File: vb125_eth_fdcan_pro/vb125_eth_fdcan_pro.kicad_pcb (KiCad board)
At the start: 4 copper layers, 105 x 82 mm, 106 parts, among them J1 TAGconnect NL, J2 ARJM11C7-114-BA-EW2, J3 USB_C_Receptacle_USB2.0, J4 D09P33E4GL00LF, J5 D09P33E4GL00LF, M1 DM-OLED042-647, M2 B0505MT-1WR4, Q1 BSS138, Q2 BSS138, Q3 FDN358P, Q4 FDN358P, SW1 DS04-254-2-03BK-SMT, U1 STM32H725IGKx, U2 LAN8740A, U3 USB3315, U4 AOZ1282CI, U6 RT5760A/B, U7 LT8304IS8E#PBF, U8 ADM3057E, U9 LTC4267, X1 50MHz, X2 24MHz

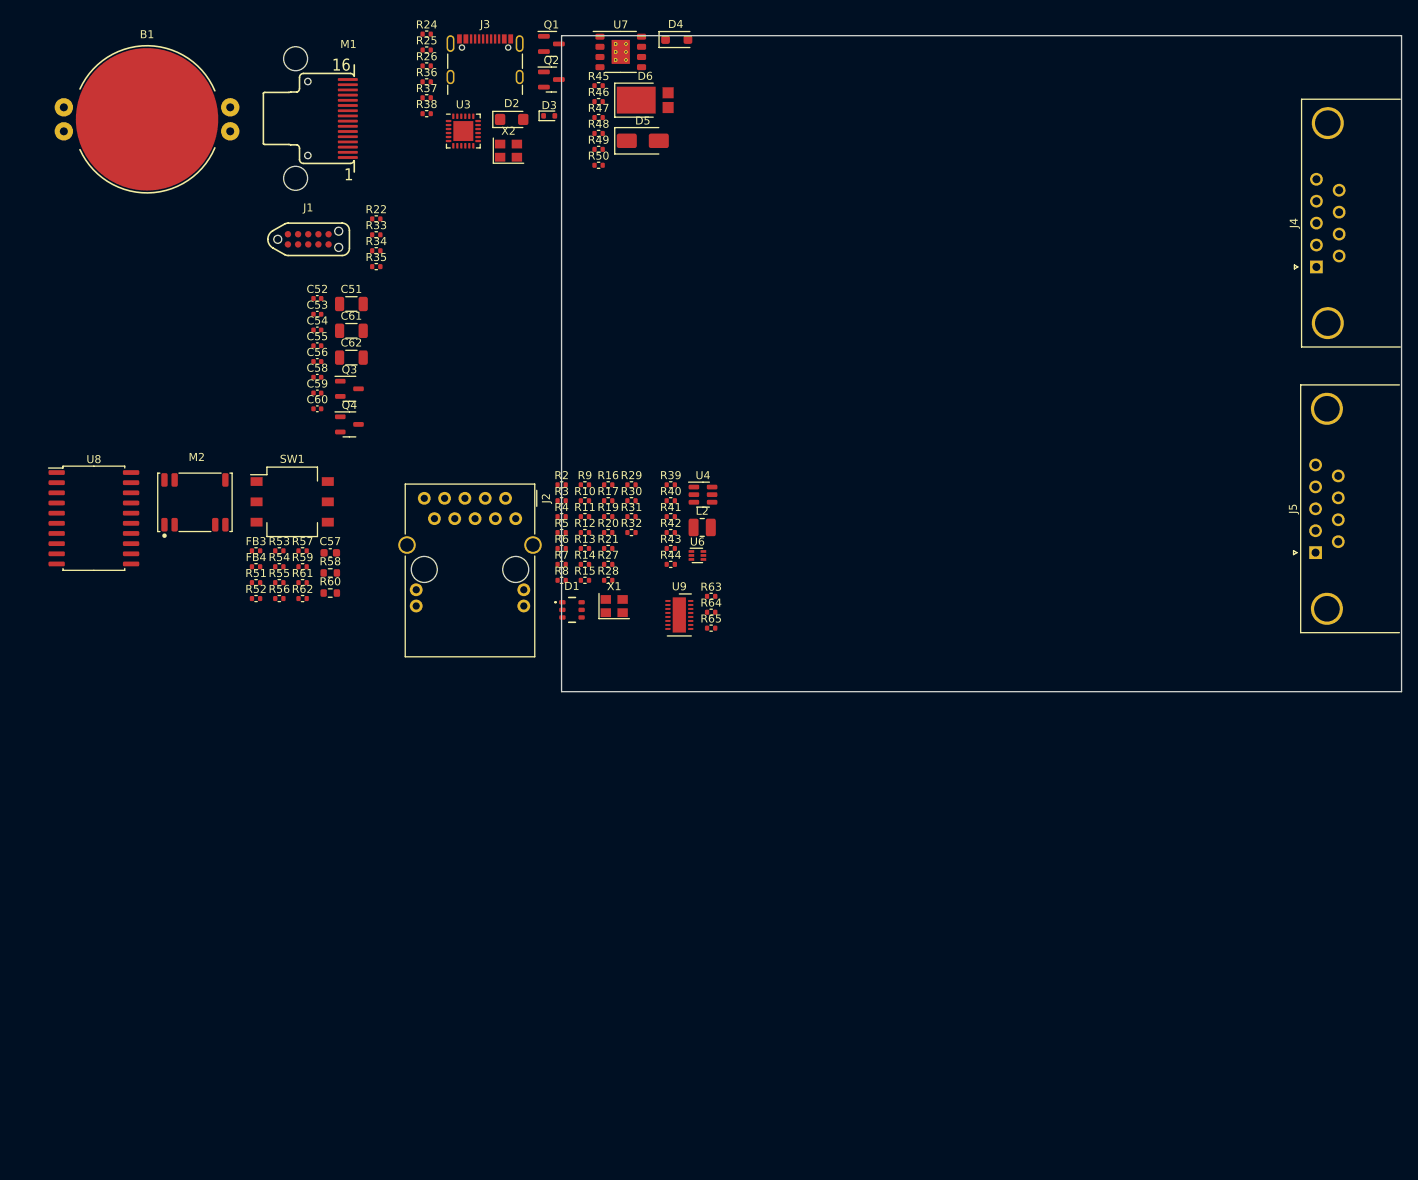
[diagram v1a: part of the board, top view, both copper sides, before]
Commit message: CAN schematics. Assign IO on H7.
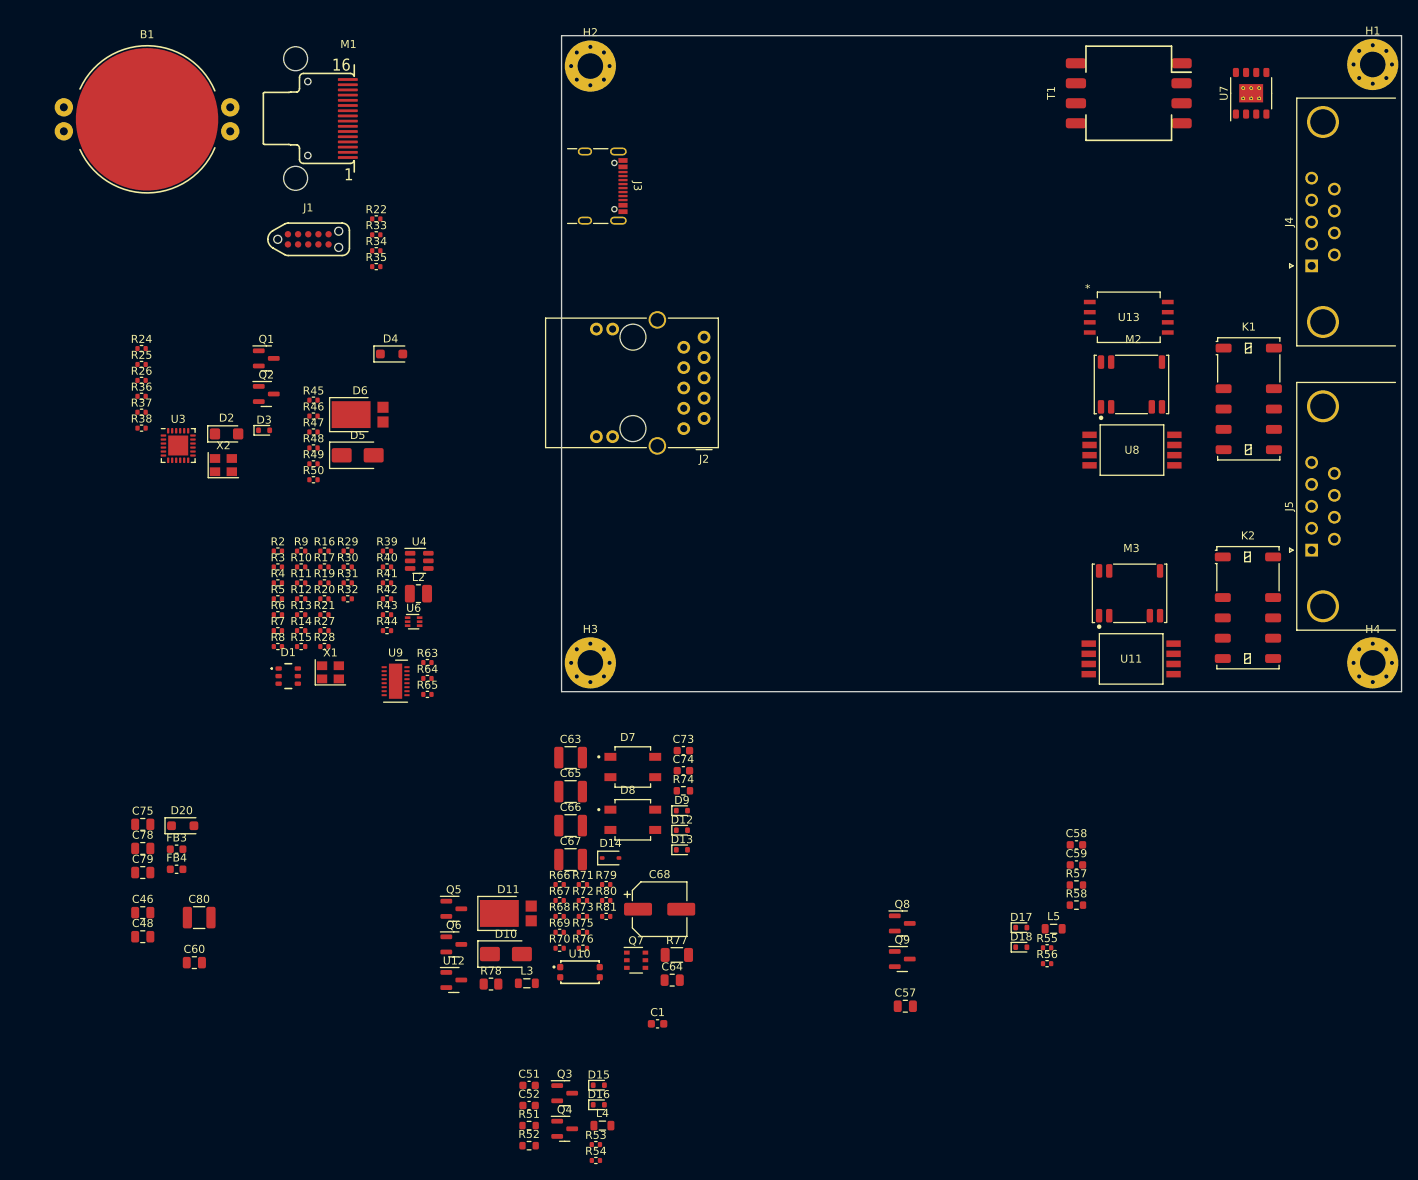
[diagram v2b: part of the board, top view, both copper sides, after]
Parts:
- removed C53, C55: X7R_10nF_50V, Capacitor_SMD:C_0402_1005Metric
- removed C54: 50V_100nF_X7R, Capacitor_SMD:C_0402_1005Metric
- removed C56: 5.0pF, Capacitor_SMD:C_0402_1005Metric
- removed C61, C62: 10.0uF ±10% 10V X7R, Capacitor_SMD:C_1206_3216Metric
- removed R59: 100K 1%, Resistor_SMD:R_0402_1005Metric
- removed R60: 56R, Resistor_SMD:R_0603_1608Metric
- removed R61, R62: 0, Resistor_SMD:R_0402_1005Metric
- removed SW1: DS04-254-2-03BK-SMT, Button_Switch_SMD:SW_DIP_SPSTx03_Slide_Omron_A6S-310x_W8.9mm_P2.54mm
- added C1: 4.7uF, Capacitor_SMD:C_0603_1608Metric, F.Cu at (161.2, 161.3)
- added C46: 10uF, Capacitor_SMD:C_0805_2012Metric, F.Cu at (96.8, 147.4)
- added C48: 10uF, Capacitor_SMD:C_0805_2012Metric, F.Cu at (96.8, 150.4)
- added C63: 4.7uF, Capacitor_SMD:C_1210_3225Metric, F.Cu at (150.3, 128.0)
- added C64: 100nF, Capacitor_SMD:C_0805_2012Metric, F.Cu at (163.0, 155.9)
- added C65: 1uF, Capacitor_SMD:C_1210_3225Metric, F.Cu at (150.3, 132.3)
- added C66: 47uF, Capacitor_SMD:C_1210_3225Metric, F.Cu at (150.3, 136.5)
- added C67: 47uF, Capacitor_SMD:C_1210_3225Metric, F.Cu at (150.3, 140.8)
- added C68: 220uF?, Capacitor_SMD:CP_Elec_6.3x7.7, F.Cu at (161.5, 147.0)
- added C73: 68pF, Capacitor_SMD:C_0603_1608Metric, F.Cu at (164.4, 127.2)
- added C74: 4.7uF, Capacitor_SMD:C_0603_1608Metric, F.Cu at (164.4, 129.7)
- added C75: 10uF, Capacitor_SMD:C_0805_2012Metric, F.Cu at (96.8, 136.4)
- added C78: DNP, Capacitor_SMD:C_0805_2012Metric, F.Cu at (96.8, 139.4)
- added C79: 10uF, Capacitor_SMD:C_0805_2012Metric, F.Cu at (96.8, 142.4)
- added C80: 10uF, Capacitor_SMD:C_1210_3225Metric, F.Cu at (103.9, 148.0)
- added D10: SMAJ58A, Diode_SMD:D_SMA, F.Cu at (142.2, 152.6)
- added D11: PDS360-13, Diode_SMD:D_PowerDI-5, F.Cu at (142.5, 147.5)
- added D12: BAS516, Diode_SMD:D_SOD-523, F.Cu at (164.2, 137.1)
- added D13: BAS516, Diode_SMD:D_SOD-523, F.Cu at (164.2, 139.6)
- added D14: MMSZ5237BS-7-F, Diode_SMD:D_SOD-323, F.Cu at (155.3, 140.6)
- added D15: BAS516, Diode_SMD:D_SOD-523, F.Cu at (153.9, 169.0)
- added D16: BAS516, Diode_SMD:D_SOD-523, F.Cu at (153.9, 171.4)
- added D17: BAS516, Diode_SMD:D_SOD-523, F.Cu at (206.7, 149.3)
- added D18: BAS516, Diode_SMD:D_SOD-523, F.Cu at (206.7, 151.7)
- added D20: RB168MM150TFTR, Diode_SMD:D_SOD-123F, F.Cu at (101.8, 136.6)
- added D7: HDS10M-13, vhrd_passive_diode:DIOB_HDS10M-13, F.Cu at (158.1, 129.2)
- added D8: HDS10M-13, vhrd_passive_diode:DIOB_HDS10M-13, F.Cu at (158.1, 135.8)
- added D9: BAS516, Diode_SMD:D_SOD-523, F.Cu at (164.2, 134.7)
- added H1: MountingHole_Pad, MountingHole:MountingHole_3.2mm_M3_Pad_Via, F.Cu at (250.6, 41.4)
- added H2: MountingHole_Pad, MountingHole:MountingHole_3.2mm_M3_Pad_Via, F.Cu at (152.8, 41.6)
- added H3: MountingHole_Pad, MountingHole:MountingHole_3.2mm_M3_Pad_Via, F.Cu at (152.8, 116.2)
- added H4: MountingHole_Pad, MountingHole:MountingHole_3.2mm_M3_Pad_Via, F.Cu at (250.6, 116.2)
- added K1: EE2-4.5TNUH, vhrd_relay:Relay_DPDT_Kemet_EE2_NUH_DoubleCoil, F.Cu at (235.1, 83.2)
- added K2: EE2-4.5TNUH, vhrd_relay:Relay_DPDT_Kemet_EE2_NUH_DoubleCoil, F.Cu at (235.0, 109.3)
- added L3: 3.3uH, Inductor_SMD:L_0805_2012Metric, F.Cu at (144.9, 156.2)
- added L4: 6.8uH, Inductor_SMD:L_0805_2012Metric, F.Cu at (154.3, 174.0)
- added L5: 6.8uH, Inductor_SMD:L_0805_2012Metric, F.Cu at (210.7, 149.4)
- added M3: B0505MT-1WR4, vhrd_module_power:B0505MT-1WR4, F.Cu at (220.2, 107.5)
- added Q5: 2N7002, Package_TO_SOT_SMD:SOT-23, F.Cu at (135.7, 146.9)
- added Q6: MMBTA42, Package_TO_SOT_SMD:SOT-23, F.Cu at (135.7, 151.4)
- added Q7: Si3440DV, Package_SO:TSOP-6_1.65x3.05mm_P0.95mm, F.Cu at (158.5, 153.4)
- added Q8: BSS138, Package_TO_SOT_SMD:SOT-23, F.Cu at (191.8, 148.8)
- added Q9: BSS138, Package_TO_SOT_SMD:SOT-23, F.Cu at (191.8, 153.2)
- added R66: 470R, Resistor_SMD:R_0402_1005Metric, F.Cu at (149.0, 143.9)
- added R67: 100K, Resistor_SMD:R_0402_1005Metric, F.Cu at (149.0, 145.9)
- added R68: 33K2, Resistor_SMD:R_0402_1005Metric, F.Cu at (149.0, 147.9)
- added R69: 47K, Resistor_SMD:R_0402_1005Metric, F.Cu at (149.0, 149.9)
- added R70: 1K, Resistor_SMD:R_0402_1005Metric, F.Cu at (149.0, 151.9)
- added R71: 10K, Resistor_SMD:R_0402_1005Metric, F.Cu at (151.9, 143.9)
- added R72: 6K8, Resistor_SMD:R_0402_1005Metric, F.Cu at (151.9, 145.9)
- added R73: 100K, Resistor_SMD:R_0402_1005Metric, F.Cu at (151.9, 147.9)
- added R74: 10R, Resistor_SMD:R_0603_1608Metric, F.Cu at (164.4, 132.2)
- added R75: DNP, Resistor_SMD:R_0402_1005Metric, F.Cu at (151.9, 149.9)
- added R76: 510R, Resistor_SMD:R_0402_1005Metric, F.Cu at (151.9, 151.9)
- added R77: 0.125R, Resistor_SMD:R_1206_3216Metric, F.Cu at (163.6, 152.7)
- added R78: 100R, Resistor_SMD:R_0805_2012Metric, F.Cu at (140.4, 156.3)
- added R79: 4K7, Resistor_SMD:R_0402_1005Metric, F.Cu at (154.8, 143.9)
- added R80: 220K, Resistor_SMD:R_0402_1005Metric, F.Cu at (154.8, 145.9)
- added R81: 220K, Resistor_SMD:R_0402_1005Metric, F.Cu at (154.8, 147.9)
- added T1: PA1134NL, vhrd_transformer:PA1134NL, F.Cu at (220.1, 45.0)
- added U10: PS2911-1-F3-AX, vhrd_opto_isolator:PS2911, F.Cu at (151.5, 154.9)
- added U11: TLP2270, vhrd_generic:SO8L_TOS, F.Cu at (220.4, 115.7)
- added U12: ZR431, Package_TO_SOT_SMD:SOT-23, F.Cu at (135.7, 155.8)
- added U13: ADM3050EBRIZ, vhrd_generic:RI-8-1_ADI, F.Cu at (220.1, 73.0)
- C51: value 10.0uF ±10% 10V X7R -> 4.7uF; footprint Capacitor_SMD:C_1206_3216Metric -> Capacitor_SMD:C_0603_1608Metric
- C52: value 50V_100nF_X7R -> 4.7uF; footprint Capacitor_SMD:C_0402_1005Metric -> Capacitor_SMD:C_0603_1608Metric
- C57: value 4.7uF ±10% 6.3V -> 10uF; footprint Capacitor_SMD:C_0603_1608Metric -> Capacitor_SMD:C_0805_2012Metric
- C58: value 10.0nF ±10% 50V X7R -> 4.7uF; footprint Capacitor_SMD:C_0402_1005Metric -> Capacitor_SMD:C_0603_1608Metric
- C59: value 0.1uF 10% X7R 50V -> 4.7uF; footprint Capacitor_SMD:C_0402_1005Metric -> Capacitor_SMD:C_0603_1608Metric
- C60: value 220.0nF ±10% 10V X7R -> 10uF; footprint Capacitor_SMD:C_0402_1005Metric -> Capacitor_SMD:C_0805_2012Metric
- D6: value PDS835L-13 -> PDS360-13
- FB3: value 100MHz_1.8KOhm -> BLM18HE152SN1D; footprint Resistor_SMD:R_0402_1005Metric -> Inductor_SMD:L_0603_1608Metric
- FB4: value BLM15BX182SN1D_100MHz_1.8KOhm -> BLM18HE152SN1D; footprint Resistor_SMD:R_0402_1005Metric -> Inductor_SMD:L_0603_1608Metric
- Q3, Q4: value FDN358P -> BSS138; footprint Package_TO_SOT_SMD:SOT-23-3 -> Package_TO_SOT_SMD:SOT-23
- R51, R57: value 0 -> 60R4; footprint Resistor_SMD:R_0402_1005Metric -> Resistor_SMD:R_0603_1608Metric
- R52: value 47K 1% -> 60R4; footprint Resistor_SMD:R_0402_1005Metric -> Resistor_SMD:R_0603_1608Metric
- R53, R55: value 0 -> 1K
- R54: value 47K 1% -> 1K
- R56: value 100K 1% -> 1K
- R58: value 56R -> 60R4
- U8: value ADM3057E -> TLP2270; footprint Package_SO:SOIC-20W_7.5x12.8mm_P1.27mm -> vhrd_generic:SO8L_TOS
- moved U8 130.0 mm to (220.5, 89.6)
- moved M2 118.0 mm to (220.4, 81.4)
- moved C59 111.7 mm to (213.6, 141.5)
- moved C58 111.4 mm to (213.6, 138.9)
- moved R55 106.3 mm to (209.9, 151.8)
- moved R56 106.3 mm to (209.9, 153.8)
- moved R57 105.4 mm to (213.6, 144.0)
- moved C52 104.3 mm to (145.1, 171.5)
- moved R58 102.1 mm to (213.6, 146.5)
- moved C51 100.2 mm to (145.1, 169.0)
- moved Q3 92.1 mm to (149.6, 170.0)
- moved Q4 92.1 mm to (149.6, 174.4)
- moved C57 91.5 mm to (192.2, 159.1)
- moved R53 84.1 mm to (153.5, 176.4)
- moved R54 84.1 mm to (153.5, 178.4)
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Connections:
- net +5V0_DCDC renamed TERM1_EN
- net Net-(D5-A) renamed +VIN_CH1
- C51 pad 1: Net-(U8-VCC) -> Net-(C51-Pad1)
- C52 pad 1: Net-(U8-VCC) -> +5V0_SYS
- C57 pad 1: Net-(C57-Pad1) -> Net-(M2-+VO)
- C57 pad 2: GND -> ISO_1
- C58 pad 1: +5V0_ISO -> +5V0_SYS
- C58 pad 2: ISO -> GND
- C59 pad 1: +5V0_ISO -> Net-(C59-Pad1)
- C59 pad 2: ISO -> GND
- C60 pad 1: Net-(U8-VISOOUT) -> +5V0_ISO_2
- C60 pad 2: ISO -> ISO_2
- FB3 pad 1: Net-(FB3-Pad1) -> +3V3_DCDC
- FB3 pad 2: ISO -> Net-(U13-VDD1)
- FB4 pad 1: Net-(U8-VISOOUT) -> Net-(M2-+VO)
- FB4 pad 2: +5V0_ISO -> +5V0_ISO_1
- J2 pad 1: unconnected-(J2-VC2--Pad1) -> POE_AC4
- J2 pad 2: unconnected-(J2-VC1--Pad2) -> POE_AC2
- J2 pad 6: unconnected-(J2-VC2+-Pad6) -> POE_AC3
- J2 pad 7: unconnected-(J2-VC1+-Pad7) -> POE_AC1
- J2 pad SH: unconnected-(J2-SHIELD-PadSH) -> CHASSIS
- J3 pad S1: unconnected-(J3-SHIELD-PadS1) -> CHASSIS
- J4 pad 0: unconnected-(J4-PAD-Pad0) -> CHASSIS
- J4 pad 1: unconnected-(J4-Pad1) -> Net-(D20-A)
- J4 pad 2: unconnected-(J4-Pad2) -> /CAN Ch1/CAN1_L
- J4 pad 3: unconnected-(J4-Pad3) -> ISO_1
- J4 pad 6: unconnected-(J4-Pad6) -> ISO_1
- J4 pad 7: unconnected-(J4-Pad7) -> /CAN Ch1/CAN1_H
- J4 pad 9: unconnected-(J4-Pad9) -> Net-(D20-A)
- J5 pad 0: unconnected-(J5-PAD-Pad0) -> CHASSIS
- M2 pad 13: Net-(C57-Pad1) -> Net-(C51-Pad1)
- M2 pad 14: Net-(C57-Pad1) -> Net-(C51-Pad1)
- M2 pad 6: ISO -> ISO_1
- M2 pad 7: ISO -> ISO_1
- M2 pad 8: +5V -> Net-(M2-+VO)
- Q3 pad 1: /CAN Ch1/TERM_EN_ISO -> /CAN Ch1/CT1_GS
- Q3 pad 2: Net-(Q3-S) -> ISO_1
- Q3 pad 3: Net-(Q3-D) -> Net-(D15-A)
- Q4 pad 1: /CAN Ch1/TERM_EN_ISO -> /CAN Ch1/CT1_GR
- Q4 pad 2: Net-(Q4-S) -> ISO_1
- Q4 pad 3: Net-(Q3-S) -> Net-(D16-A)
- R46 pad 2: ISO -> ISO_1
- R47 pad 2: ISO -> ISO_1
- R51 pad 1: +3V3_DCDC -> /CAN Ch1/CAN1_H
- R51 pad 2: Net-(U8-VCC) -> Net-(K1-Pad5)
- R52 pad 1: Net-(R52-Pad1) -> /CAN Ch1/CAN1_L
- R52 pad 2: ISO -> Net-(K1-Pad8)
- R53 pad 2: Net-(U8-VCC) -> /CAN Ch1/CT1_AS
- R54 pad 1: Net-(R54-Pad1) -> TERM1_DIS
- R54 pad 2: ISO -> /CAN Ch1/CT1_AR
- R55 pad 1: +3V3_DCDC -> TERM2_EN
- R55 pad 2: Net-(U8-VIO) -> /CAN Ch2/CT2_AS
- R56 pad 1: /CAN Ch1/TERM_EN_ISO -> TERM2_DIS
- R56 pad 2: ISO -> /CAN Ch2/CT2_AR
- R57 pad 1: Net-(U8-VIO) -> unconnected-(R57-Pad1)
- R57 pad 2: GND -> Net-(K2-Pad5)
- R58 pad 1: /CAN Ch1/CANL -> unconnected-(R58-Pad1)
- R58 pad 2: Net-(Q3-D) -> Net-(K2-Pad8)
- R63 pad 1: GND -> ISO_POE
- R64 pad 1: GND -> ISO_POE
- R65 pad 1: GND -> ISO_POE
- U7 pad 4: ISO -> ISO_1
- U7 pad 9: ISO -> ISO_1
- U8 pad 1: GND -> /CAN Ch1/CT1_AS
- U8 pad 3: Net-(U8-VCC) -> GND
- U8 pad 4: Net-(U8-VIO) -> /CAN Ch1/CT1_AR
- U8 pad 5: CAN1_RXD -> ISO_1
- U8 pad 6: CAN1_SILENT -> /CAN Ch1/CT1_GR
- U8 pad 7: CAN1_TXD -> /CAN Ch1/CT1_GS
- U8 pad 8: CAN1_STBY -> +5V0_ISO_1
- U9 pad 1: unconnected-(U9-ITH/RUN-Pad1) -> /PoE/POE_ITH
- U9 pad 10: unconnected-(U9-POUT-Pad10) -> ISO_POE
- U9 pad 11: unconnected-(U9-~{PWRGD}-Pad11) -> /PoE/~{POE_PWRGD}
- U9 pad 12: unconnected-(U9-SIGDISA-Pad12) -> /PoE/POE_BR_N
- U9 pad 13: unconnected-(U9-VPORTP-Pad13) -> /PoE/POE_VPORTP
- U9 pad 14: unconnected-(U9-SENSE-Pad14) -> /PoE/POE_ISENSE
- U9 pad 15: unconnected-(U9-PGND-Pad15) -> ISO_POE
- U9 pad 16: unconnected-(U9-VFB-Pad16) -> ISO_POE
- U9 pad 17: unconnected-(U9-EP_PGND-Pad17) -> /PoE/POE_EP_THPAD
- U9 pad 2: unconnected-(U9-PGND-Pad2) -> ISO_POE
- U9 pad 3: unconnected-(U9-NGATE-Pad3) -> /PoE/POE_NGATE
- U9 pad 4: unconnected-(U9-PVCC-Pad4) -> /PoE/POE_PVCC
- U9 pad 5: unconnected-(U9-RCLASS-Pad5) -> Net-(U9-RCLASS)
- U9 pad 7: unconnected-(U9-VPORTN-Pad7) -> /PoE/POE_BR_N

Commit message: Finish schematics.
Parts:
- removed Q8, Q9: BSS138, Package_TO_SOT_SMD:SOT-23
- added C10: 4.7uF, Capacitor_SMD:C_0402_1005Metric, F.Cu at (41.7, 110.0)
- added C100: 1uF, Capacitor_SMD:C_0402_1005Metric, F.Cu at (71.5, 136.3)
- added C101: Y rated, THT, Capacitor_THT:C_Disc_D7.0mm_W2.5mm_P5.00mm, F.Cu at (35.2, 134.5)
- added C102: Y rated, THT, Capacitor_THT:C_Disc_D7.0mm_W2.5mm_P5.00mm, F.Cu at (58.4, 129.4)
- added C103: Y rated, SMD 1808, vhrd_generic:C_1808_4520Metric, F.Cu at (37.0, 139.0)
- added C104: Y rated, SMD 1808, vhrd_generic:C_1808_4520Metric, F.Cu at (60.1, 133.9)
- added C105: 100nF, Capacitor_SMD:C_0402_1005Metric, F.Cu at (72.4, 116.3)
- added C106: 100nF, Capacitor_SMD:C_0402_1005Metric, F.Cu at (72.4, 118.3)
- added C107: 4.7uF, Capacitor_SMD:C_1210_3225Metric, F.Cu at (56.5, 105.2)
- added C108: 4.7uF, Capacitor_SMD:C_1210_3225Metric, F.Cu at (56.5, 109.4)
- added C109: 4.7uF, Capacitor_SMD:C_1210_3225Metric, F.Cu at (56.5, 113.7)
- added C11: 100nF, Capacitor_SMD:C_0402_1005Metric, F.Cu at (41.7, 111.9)
- added C110: 4.7uF, Capacitor_SMD:C_1210_3225Metric, F.Cu at (56.5, 117.9)
- added C111: 100nF, Capacitor_SMD:C_0402_1005Metric, F.Cu at (72.4, 120.3)
- added C112: 100uF, Capacitor_SMD:C_1210_3225Metric, F.Cu at (56.5, 122.2)
- added C113: Y rated, THT, Capacitor_THT:C_Disc_D7.0mm_W2.5mm_P5.00mm, F.Cu at (21.4, 142.1)
- added C114: Y rated, SMD 1808, vhrd_generic:C_1808_4520Metric, F.Cu at (23.1, 146.6)
- added C12: 2.2uF, Capacitor_SMD:C_0402_1005Metric, F.Cu at (41.7, 113.9)
- added C13: 100nF, Capacitor_SMD:C_0402_1005Metric, F.Cu at (41.7, 115.9)
- added C14: 4.7uF, Capacitor_SMD:C_0402_1005Metric, F.Cu at (44.5, 104.0)
- added C15: 10nF, Capacitor_SMD:C_0402_1005Metric, F.Cu at (71.5, 144.2)
- added C16: 10nF, Capacitor_SMD:C_0402_1005Metric, F.Cu at (68.6, 128.4)
- added C17: 22nF, Capacitor_SMD:C_0402_1005Metric, F.Cu at (74.3, 140.3)
- added C18: 100nF, Capacitor_SMD:C_0402_1005Metric, F.Cu at (74.3, 142.2)
- added C19: 4.7uF, Capacitor_SMD:C_0402_1005Metric, F.Cu at (74.3, 144.2)
- added C2: 100nF, Capacitor_SMD:C_0402_1005Metric, F.Cu at (41.7, 104.0)
- added C20: 100nF, Capacitor_SMD:C_0402_1005Metric, F.Cu at (44.5, 106.0)
- added C21: 100nF, Capacitor_SMD:C_0402_1005Metric, F.Cu at (44.5, 108.0)
- added C22: 100nF, Capacitor_SMD:C_0402_1005Metric, F.Cu at (44.5, 110.0)
- added C23: 100nF, Capacitor_SMD:C_0402_1005Metric, F.Cu at (44.5, 111.9)
- added C24: 100nF, Capacitor_SMD:C_0402_1005Metric, F.Cu at (44.5, 113.9)
- added C25: 100nF, Capacitor_SMD:C_0402_1005Metric, F.Cu at (44.5, 115.9)
- added C26: 100nF, Capacitor_SMD:C_0402_1005Metric, F.Cu at (47.4, 104.0)
- added C27: 100nF, Capacitor_SMD:C_0402_1005Metric, F.Cu at (47.4, 106.0)
- added C28: 100nF, Capacitor_SMD:C_0402_1005Metric, F.Cu at (47.4, 108.0)
- added C29: 100nF, Capacitor_SMD:C_0402_1005Metric, F.Cu at (47.4, 110.0)
- added C3: 100nF, Capacitor_SMD:C_0402_1005Metric, F.Cu at (68.6, 140.3)
- added C30: 1uF, Capacitor_SMD:C_0402_1005Metric, F.Cu at (47.4, 111.9)
- added C31: 4.7uF, Capacitor_SMD:C_0402_1005Metric, F.Cu at (47.4, 113.9)
- added C32: 4.7uF, Capacitor_SMD:C_0402_1005Metric, F.Cu at (47.4, 115.9)
- added C33: 220pF, Capacitor_SMD:C_0402_1005Metric, F.Cu at (50.3, 104.0)
- added C34: 10uF, Capacitor_SMD:C_0402_1005Metric, F.Cu at (50.3, 106.0)
- added C35: 10uF, Capacitor_SMD:C_0402_1005Metric, F.Cu at (50.3, 108.0)
- added C36: 1uF, Capacitor_SMD:C_0402_1005Metric, F.Cu at (50.3, 110.0)
- added C37: 100nF, Capacitor_SMD:C_0402_1005Metric, F.Cu at (50.3, 111.9)
- added C38: 10nF, Capacitor_SMD:C_0402_1005Metric, F.Cu at (68.6, 130.4)
- added C39: 10nF, Capacitor_SMD:C_0402_1005Metric, F.Cu at (68.6, 132.3)
- added C4: 100nF, Capacitor_SMD:C_0402_1005Metric, F.Cu at (68.6, 142.2)
- added C40: 10nF, Capacitor_SMD:C_0402_1005Metric, F.Cu at (68.6, 134.3)
- added C41: 10nF, Capacitor_SMD:C_0402_1005Metric, F.Cu at (68.6, 136.3)
- added C42: 3.3nF, Capacitor_SMD:C_0402_1005Metric, F.Cu at (55.2, 142.2)
- added C43: >10uF, Capacitor_SMD:C_0603_1608Metric, F.Cu at (58.6, 142.5)
- added C44: DNP, Capacitor_SMD:C_0603_1608Metric, F.Cu at (58.6, 145.0)
- added C45: 100nF, Capacitor_SMD:C_0402_1005Metric, F.Cu at (55.2, 144.2)
- added C47: DNP, Capacitor_SMD:C_0402_1005Metric, F.Cu at (55.2, 146.2)
- added C49: 1uF, Capacitor_SMD:C_0402_1005Metric, F.Cu at (72.4, 114.3)
- added C5: 100nF, Capacitor_SMD:C_0402_1005Metric, F.Cu at (68.6, 144.2)
- added C50: 220pF, Capacitor_SMD:C_0603_1608Metric, F.Cu at (70.5, 106.7)
- added C53: 4n7, Capacitor_SMD:C_0402_1005Metric, F.Cu at (32.0, 133.5)
- added C54: 100nF, Capacitor_SMD:C_0402_1005Metric, F.Cu at (32.0, 135.5)
- added C55: DNP, Capacitor_SMD:C_0805_2012Metric, F.Cu at (41.7, 36.8)
- added C56: 10uF, Capacitor_SMD:C_0805_2012Metric, F.Cu at (41.7, 39.8)
- added C6: 1uF, Capacitor_SMD:C_0402_1005Metric, F.Cu at (71.5, 140.3)
- added C61: 100nF, Capacitor_SMD:C_0402_1005Metric, F.Cu at (32.0, 137.4)
- added C62: 10nF, Capacitor_SMD:C_0402_1005Metric, F.Cu at (32.0, 139.4)
- added C69: 33nF, Capacitor_SMD:C_0402_1005Metric, F.Cu at (45.5, 133.5)
- added C7: 470pF, Capacitor_SMD:C_0402_1005Metric, F.Cu at (71.5, 142.2)
- added C70: 1uF, Capacitor_SMD:C_0402_1005Metric, F.Cu at (45.5, 135.5)
- added C71: 27nF, Capacitor_SMD:C_0402_1005Metric, F.Cu at (45.5, 137.4)
- added C72: 470pF, Capacitor_SMD:C_0402_1005Metric, F.Cu at (45.5, 139.4)
- added C76: 10nF, Capacitor_SMD:C_0402_1005Metric, F.Cu at (32.0, 141.4)
- added C77: 100nF, Capacitor_SMD:C_0402_1005Metric, F.Cu at (32.0, 143.3)
- added C8: 1uF, Capacitor_SMD:C_0402_1005Metric, F.Cu at (41.7, 106.0)
- added C81: 4.7uF, Capacitor_SMD:C_0603_1608Metric, F.Cu at (17.7, 93.7)
- added C82: 100nF, Capacitor_SMD:C_0402_1005Metric, F.Cu at (50.3, 113.9)
- added C83: 12pF, Capacitor_SMD:C_0402_1005Metric, F.Cu at (24.3, 86.1)
- added C84: 12pF, Capacitor_SMD:C_0402_1005Metric, F.Cu at (24.3, 88.1)
- added C85: 1uF, Capacitor_SMD:C_0402_1005Metric, F.Cu at (71.5, 128.4)
- added C86: 100nF, Capacitor_SMD:C_0402_1005Metric, F.Cu at (71.5, 130.4)
- added C87: 4.7uF, Capacitor_SMD:C_0603_1608Metric, F.Cu at (53.8, 36.6)
- added C88: 100nF, Capacitor_SMD:C_0402_1005Metric, F.Cu at (71.5, 132.3)
- added C89: 100uF, Capacitor_SMD:C_1210_3225Metric, F.Cu at (55.7, 77.3)
- added C9: 1uF, Capacitor_SMD:C_0402_1005Metric, F.Cu at (41.7, 108.0)
- added C90: 100uF, Capacitor_SMD:C_1210_3225Metric, F.Cu at (55.7, 81.5)
- added C91: 100uF, Capacitor_SMD:C_1210_3225Metric, F.Cu at (55.7, 85.8)
- added C92: 4.7uF, Capacitor_SMD:C_0603_1608Metric, F.Cu at (18.4, 60.4)
- added C93: 100nF, Capacitor_SMD:C_0402_1005Metric, F.Cu at (55.2, 132.3)
- added C94: 10nF, Capacitor_SMD:C_0402_1005Metric, F.Cu at (55.2, 134.3)
- added C95: 10uF, Capacitor_SMD:C_0805_2012Metric, F.Cu at (41.7, 42.9)
- added C96: 100nF, Capacitor_SMD:C_0402_1005Metric, F.Cu at (55.2, 136.3)
- added C97: 10uF, Capacitor_SMD:C_0805_2012Metric, F.Cu at (41.7, 45.9)
- added C98: 4n7, Capacitor_SMD:C_0402_1005Metric, F.Cu at (55.2, 138.3)
- added C99: 1uF, Capacitor_SMD:C_0402_1005Metric, F.Cu at (71.5, 134.3)
- added D21: buspower_iso: SMAJ58CA; buspower_dc: SMAJ36CA, Diode_SMD:D_SMA, F.Cu at (235.2, 52.4)
- added D23: PDS360-13, Diode_SMD:D_PowerDI-5, F.Cu at (63.7, 116.2)
- added FB1: MH1608-601Y, Inductor_SMD:L_0603_1608Metric, F.Cu at (69.2, 146.4)
- added FB2: FBMJ1608HM180NTR, Inductor_SMD:L_0603_1608Metric, F.Cu at (42.2, 118.1)
- added FB5: BLM18HE152SN1D, Inductor_SMD:L_0603_1608Metric, F.Cu at (18.4, 62.9)
- added FB6: BLM18HE152SN1D, Inductor_SMD:L_0603_1608Metric, F.Cu at (18.4, 65.4)
- added J6: MEM2061-01-188-00-A, vhrd_connector_gct:MEM2061, F.Cu at (202.7, 111.8)
- added J7: Conn_02x20_Pin, Connector_PinHeader_1.27mm:PinHeader_2x20_P1.27mm_Vertical_SMD, F.Cu at (35.4, 116.8)
- added JP1: Jumper board, vhrd_generic:PCB_JUMPER, F.Cu at (65.0, 104.3)
- added L6: LMLP07A7M8R2DTAS, vhrd_inductor:LMLP07A7, F.Cu at (64.0, 109.4)
- added R1: 10K, Resistor_SMD:R_0402_1005Metric, F.Cu at (45.7, 117.8)
- added R18: 10k, Resistor_SMD:R_0402_1005Metric, F.Cu at (72.6, 146.2)
- added R23: 10k, Resistor_SMD:R_0402_1005Metric, F.Cu at (74.3, 132.3)
- added R59: 3K3, Resistor_SMD:R_0402_1005Metric, F.Cu at (24.3, 76.2)
- added R60: 3K3, Resistor_SMD:R_0402_1005Metric, F.Cu at (24.3, 78.1)
- added R61: 3K3, Resistor_SMD:R_0402_1005Metric, F.Cu at (24.3, 80.1)
- added R62: 3K3, Resistor_SMD:R_0402_1005Metric, F.Cu at (24.3, 82.1)
- added R82: 3K3, Resistor_SMD:R_0402_1005Metric, F.Cu at (24.3, 84.1)
- added R83: 3K3, Resistor_SMD:R_0402_1005Metric, F.Cu at (27.2, 76.2)
- added R84: 3K3, Resistor_SMD:R_0402_1005Metric, F.Cu at (27.2, 78.1)
- added R85: 3K3, Resistor_SMD:R_0402_1005Metric, F.Cu at (27.2, 80.1)
- added R86: 3K3, Resistor_SMD:R_0402_1005Metric, F.Cu at (27.2, 82.1)
- added R87: 3K3, Resistor_SMD:R_0402_1005Metric, F.Cu at (27.2, 84.1)
- added R88: 33R, Resistor_SMD:R_0402_1005Metric, F.Cu at (30.1, 76.2)
- added R89: 10K, Resistor_SMD:R_0402_1005Metric, F.Cu at (30.1, 78.1)
- added R90: 10K, Resistor_SMD:R_0402_1005Metric, F.Cu at (30.1, 80.1)
- added R91: 10K, Resistor_SMD:R_0402_1005Metric, F.Cu at (50.3, 38.3)
- added R92: 39R, Resistor_SMD:R_0402_1005Metric, F.Cu at (50.3, 40.3)
- added R93: 10K, Resistor_SMD:R_0402_1005Metric, F.Cu at (50.3, 42.3)
- added R94: 250R, Resistor_SMD:R_0603_1608Metric, F.Cu at (70.5, 109.2)
- added R95: 10K, Resistor_SMD:R_0402_1005Metric, F.Cu at (69.5, 114.4)
- added R96: 49K9, Resistor_SMD:R_0402_1005Metric, F.Cu at (69.5, 116.3)
- added R97: 10K, Resistor_SMD:R_0402_1005Metric, F.Cu at (69.5, 118.3)
- added R98: 57K6, Resistor_SMD:R_0402_1005Metric, F.Cu at (69.5, 120.3)
- added SW1: KSS331GLFS, vhrd_electromechanical:SW_KSS3, F.Cu at (189.2, 116.8)
- added T2: 750315125, vhrd_transformer:750315125, F.Cu at (211.8, 41.0)
- added U14: TLP2270, vhrd_generic:SO8L_TOS, F.Cu at (220.0, 89.8)
- added U15: NCP563SQ18T1G, Package_TO_SOT_SMD:SC-82AB, F.Cu at (74.9, 129.3)
- C58: value 4.7uF -> 100nF; footprint Capacitor_SMD:C_0603_1608Metric -> Capacitor_SMD:C_0402_1005Metric
- C60: value 10uF -> 10nF; footprint Capacitor_SMD:C_0805_2012Metric -> Capacitor_SMD:C_0402_1005Metric
- D3: value MM5Z10VT1G -> 5V6?; footprint Diode_SMD:D_SOD-523 -> Diode_SMD:D_SOD-323
- M1: moved to B.Cu
- R38: value 5K1 -> 39R
- U11: value TLP2270 -> ADM3050EBRIZ; footprint vhrd_generic:SO8L_TOS -> vhrd_generic:RI-8-1_ADI
- U4: value AOZ1282CI -> LV14360SDDAR; footprint Package_TO_SOT_SMD:SOT-23-6 -> Package_SO:SOIC-8-1EP_3.9x4.9mm_P1.27mm_EP2.95x4.9mm_Mask2.71x3.4mm_ThermalVias
- moved C59 212.3 mm to (18.4, 57.9)
- moved R57 209.4 mm to (18.4, 67.9)
- moved R58 209.4 mm to (18.4, 70.4)
- moved D17 188.7 mm to (36.3, 68.2)
- moved D18 188.7 mm to (36.3, 70.7)
- moved L5 188.7 mm to (40.3, 68.3)
- moved R55 185.8 mm to (44.1, 68.0)
- moved R56 185.8 mm to (44.1, 70.0)
- moved C58 158.8 mm to (55.2, 128.4)
- moved M1 78.2 mm to (172.6, 108.2), turned to 90 degrees
- moved D3 76.4 mm to (35.8, 91.5)
- moved Q1 75.9 mm to (42.0, 49.6)
- moved Q2 75.9 mm to (42.0, 54.0)
- moved U4 70.4 mm to (63.6, 122.2)
- moved R38 68.6 mm to (50.3, 36.3)
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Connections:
- net +5V0_ISO_1 renamed /CAN Ch1/+5V0_ISO
- net /CAN Ch1/CAN1_H renamed /CAN Ch1/CAN_H
- net /CAN Ch1/CAN1_L renamed /CAN Ch1/CAN_L
- net /CAN Ch1/CT1_AR renamed /CAN Ch1/CT_AR
- net /CAN Ch1/CT1_AS renamed /CAN Ch1/CT_AS
- net /CAN Ch1/CT1_GR renamed /CAN Ch1/CT_GR
- net /CAN Ch1/CT1_GS renamed /CAN Ch1/CT_GS
- net Net-(D20-A) renamed /Bus Power/+VIN_DB9
- net Net-(D4-A) renamed /Bus Power/BP_SW
- net Net-(M2-+VO) renamed /CAN Ch1/+VO
- C57 pad 2: ISO_1 -> /CAN Ch1/ISO
- C58 pad 1: +5V0_SYS -> Net-(U11-VDD1)
- C59 pad 1: Net-(C59-Pad1) -> +5V0_SYS
- C60 pad 1: +5V0_ISO_2 -> Net-(U11-VDD1)
- C60 pad 2: ISO_2 -> GND
- C79 pad 2: ISO_1 -> /CAN Ch1/ISO
- C80 pad 1: +VIN_CH1 -> /Bus Power/+VIN_DB9_PR
- D17 pad 1: +5V0_ISO_2 -> /CAN Ch2/+5V0_ISO
- D18 pad 1: +5V0_ISO_2 -> /CAN Ch2/+5V0_ISO
- D20 pad 1: +VIN_CH1 -> /Bus Power/+VIN_DB9_PR
- D3 pad 1: /USB/~{PD_MOD_PRES} -> +5V0_SYS
- D5 pad 2: +VIN_CH1 -> /Bus Power/+VIN_DB9_PR
- D6 pad 1: unconnected-(D6-K-Pad1) -> +5V0_SYS
- D6 pad 2: unconnected-(D6-A-Pad2) -> Net-(D6-A)
- J1 pad 8: unconnected-(J1-Pad8) -> /MCU_H7/BOOT0
- J4 pad 3: ISO_1 -> /CAN Ch1/ISO
- J4 pad 6: ISO_1 -> /CAN Ch1/ISO
- J5 pad 1: unconnected-(J5-Pad1) -> /CAN Ch2/+VIN_DB9
- J5 pad 2: unconnected-(J5-Pad2) -> /CAN Ch2/CAN_L
- J5 pad 3: unconnected-(J5-Pad3) -> /CAN Ch2/ISO
- J5 pad 6: unconnected-(J5-Pad6) -> /CAN Ch2/ISO
- J5 pad 7: unconnected-(J5-Pad7) -> /CAN Ch2/CAN_H
- J5 pad 9: unconnected-(J5-Pad9) -> /CAN Ch2/+VIN_DB9
- K2 pad 1: +5V0_ISO_2 -> /CAN Ch2/+5V0_ISO
- K2 pad 6: +5V0_ISO_2 -> /CAN Ch2/+5V0_ISO
- L5 pad 2: Net-(C59-Pad1) -> Net-(C92-Pad1)
- M1 pad 1: unconnected-(M1-C2P-Pad1) -> Net-(M1-C2P)
- M1 pad 10: unconnected-(M1-~{RESET}-Pad10) -> /MCU_H7/OLED_RST
- M1 pad 12: unconnected-(M1-D0-Pad12) -> /MCU_H7/I2C2_SCL
- M1 pad 13: Net-(M1-D1) -> /MCU_H7/I2C2_SDA
- M1 pad 14: Net-(M1-D1) -> /MCU_H7/I2C2_SDA
- M1 pad 2: unconnected-(M1-C2N-Pad2) -> Net-(M1-C2N)
- M1 pad 3: unconnected-(M1-C1P-Pad3) -> Net-(M1-C1P)
- M1 pad 4: unconnected-(M1-C1N-Pad4) -> Net-(M1-C1N)
- M1 pad 6: unconnected-(M1-VSS-Pad6) -> GND
- M2 pad 6: ISO_1 -> /CAN Ch1/ISO
- M2 pad 7: ISO_1 -> /CAN Ch1/ISO
- M3 pad 13: Net-(C59-Pad1) -> Net-(C92-Pad1)
- M3 pad 14: Net-(C59-Pad1) -> Net-(C92-Pad1)
- M3 pad 6: ISO_2 -> /CAN Ch2/ISO
- M3 pad 7: ISO_2 -> /CAN Ch2/ISO
- M3 pad 8: +5V0_ISO_2 -> /CAN Ch2/+VO
- Q1 pad 1: /USB/~{PD_MOD_PRES} -> /CAN Ch2/CT_GS
- Q1 pad 2: GND -> /CAN Ch2/ISO
- Q1 pad 3: Net-(Q1-D) -> Net-(D17-A)
- Q2 pad 1: /USB/~{PD_MOD_PRES} -> /CAN Ch2/CT_GR
- Q2 pad 2: GND -> /CAN Ch2/ISO
- Q2 pad 3: Net-(Q2-D) -> Net-(D18-A)
- Q3 pad 2: ISO_1 -> /CAN Ch1/ISO
- Q4 pad 2: ISO_1 -> /CAN Ch1/ISO
- R36 pad 2: Net-(Q1-D) -> GND
- R37 pad 2: Net-(Q2-D) -> GND
- R38 pad 1: +VIN_USB -> /USB/DM
- R38 pad 2: /USB/~{PD_MOD_PRES} -> USBFS_DM
- R45 pad 1: +VIN_CH1 -> /Bus Power/+VIN_DB9_PR
- R53 pad 1: TERM1_EN -> /CAN Ch1/TERM_EN
- R54 pad 1: TERM1_DIS -> /CAN Ch1/TERM_DIS
- R55 pad 1: TERM2_EN -> /CAN Ch2/TERM_EN
- R55 pad 2: /CAN Ch2/CT2_AS -> /CAN Ch2/CT_AS
- R56 pad 1: TERM2_DIS -> /CAN Ch2/TERM_DIS
- R56 pad 2: /CAN Ch2/CT2_AR -> /CAN Ch2/CT_AR
- R57 pad 1: unconnected-(R57-Pad1) -> /CAN Ch2/CAN_H
- R58 pad 1: unconnected-(R58-Pad1) -> /CAN Ch2/CAN_L
- U1 pad A10: FDCAN1_TX -> /CAN Ch2/FDCAN_TX
- U1 pad A11: unconnected-(U1A-PA15-PadA11) -> /MCU_H7/SPI1_NSS
- U1 pad A2: FDCAN1_RX -> /CAN Ch2/FDCAN_RX
- U1 pad A5: unconnected-(U1B-PB6-PadA5) -> /MCU_H7/USART1_TX
- U1 pad A6: unconnected-(U1B-PB3-PadA6) -> /MCU_H7/SPI1_SCK
- U1 pad A8: FDCAN3_TX -> /CAN Ch1/FDCAN_TX
- U1 pad A9: unconnected-(U1D-PD3-PadA9) -> /MCU_H7/SPI2_SCK
- U1 pad B10: SDMMC_CMD -> /MCU_H7/SDMMC_CMD
- U1 pad B11: SDMMC_CK -> /MCU_H7/SDMMC_CK
- U1 pad B15: unconnected-(U1A-PA12-PadB15) -> USBFS_DP
- U1 pad B3: unconnected-(U1B-PB9-PadB3) -> /MCU_H7/SPI2_NSS
- U1 pad B5: unconnected-(U1B-PB7-PadB5) -> /MCU_H7/USART1_RX
- U1 pad B6: unconnected-(U1B-PB4-PadB6) -> /MCU_H7/SPI1_MISO
- U1 pad B8: unconnected-(U1D-PD7-PadB8) -> /MCU_H7/SPI1_MOSI
- U1 pad B9: unconnected-(U1D-PD5-PadB9) -> /MCU_H7/USART2_TX
- U1 pad C11: SDMMC_D3 -> /MCU_H7/SDMMC_D3
- U1 pad C12: SDMMC_D2 -> /MCU_H7/SDMMC_D2
- U1 pad C15: unconnected-(U1A-PA11-PadC15) -> USBFS_DM
- U1 pad C3: unconnected-(U1E-PE2-PadC3) -> /MCU_H7/OCTOSPI_IO2
- U1 pad C8: FDCAN3_RX -> /CAN Ch1/FDCAN_RX
- U1 pad C9: unconnected-(U1D-PD4-PadC9) -> /MCU_H7/OCTOSPI_IO4
- U1 pad D1: unconnected-(U1C-PC15-OSC32_OUT-PadD1) -> /MCU_H7/OSC32_OUT
- U1 pad D14: SDMMC_D0 -> /MCU_H7/SDMMC_D0
- U1 pad D2: unconnected-(U1C-PC14-OSC32_IN-PadD2) -> /MCU_H7/OSC32_IN
- U1 pad D8: unconnected-(U1G-PG12-PadD8) -> ULPI_RST
- U1 pad D9: unconnected-(U1D-PD6-PadD9) -> /MCU_H7/USART2_RX
- U1 pad E13: SDMMC_D1 -> /MCU_H7/SDMMC_D1
- U1 pad F14: unconnected-(U1G-PG6-PadF14) -> /MCU_H7/OCTOSPI_NCS
- U1 pad F15: unconnected-(U1G-PG5-PadF15) -> /MCU_H7/BUTTON
- U1 pad F3: unconnected-(U1F-PF1-PadF3) -> /MCU_H7/I2C2_SCL
- U1 pad F4: unconnected-(U1F-PF0-PadF4) -> /MCU_H7/I2C2_SDA
- U1 pad G12: unconnected-(U1G-PG8-PadG12) -> /CAN Ch1/TERM_DIS
- U1 pad G13: unconnected-(U1G-PG7-PadG13) -> /CAN Ch1/TERM_EN
- U1 pad G14: unconnected-(U1G-PG4-PadG14) -> /MCU_H7/SDMMC_PRESENT
- U1 pad G15: unconnected-(U1G-PG2-PadG15) -> RJ45_LEDG
- U1 pad G3: unconnected-(U1F-PF2-PadG3) -> /MCU_H7/OLED_RST
- U1 pad H1: unconnected-(U1F-PF6-PadH1) -> /MCU_H7/OCTOSPI_IO3
- U1 pad H13: unconnected-(U1G-PG3-PadH13) -> RJ45_LEDY
- U1 pad J2: unconnected-(U1F-PF8-PadJ2) -> /MCU_H7/OCTOSPI_IO0
- U1 pad J4: unconnected-(U1F-PF9-PadJ4) -> /MCU_H7/OCTOSPI_IO1
- U1 pad K13: unconnected-(U1D-PD9-PadK13) -> /CAN Ch2/TERM_DIS
- U1 pad K14: unconnected-(U1B-PB15-PadK14) -> /MCU_H7/SPI2_MOSI
- U1 pad K15: unconnected-(U1B-PB14-PadK15) -> /MCU_H7/SPI2_MISO
- U1 pad K3: unconnected-(U1F-PF10-PadK3) -> /MCU_H7/OCTOSPI_CLK
- U1 pad L14: unconnected-(U1D-PD8-PadL14) -> /CAN Ch2/TERM_EN
- U1 pad M11: unconnected-(U1H-PH7-PadM11) -> /MCU_H7/I2C3_SCL
- U1 pad N13: unconnected-(U1H-PH8-PadN13) -> /MCU_H7/I2C3_SDA
- U1 pad N7: unconnected-(U1F-PF11-PadN7) -> /MCU_H7/RID_BOM
- U1 pad N8: unconnected-(U1E-PE8-PadN8) -> /MCU_H7/OCTOSPI_IO5
- U1 pad N9: unconnected-(U1G-PG1-PadN9) -> ~{ETH_PHY_RST}
- U1 pad P3: unconnected-(U1A-PA1_C-PadP3) -> /MCU_H7/RID_PRODUCT
- U1 pad P7: unconnected-(U1B-PB2-PadP7) -> /MCU_H7/OCTOSPI_DQS
- U1 pad P8: unconnected-(U1G-PG0-PadP8) -> ~{ETH_INT_PME}
- U1 pad R11: unconnected-(U1E-PE9-PadR11) -> /MCU_H7/OCTOSPI_IO6
- U1 pad R7: unconnected-(U1A-PA6-PadR7) -> /MCU_H7/RID_REV
- U1 pad R9: unconnected-(U1E-PE10-PadR9) -> /MCU_H7/OCTOSPI_IO7
- U11 pad 1: /CAN Ch2/CT2_AS -> Net-(U11-VDD1)
- U11 pad 2: GND -> /CAN Ch2/FDCAN_TX
- U11 pad 3: GND -> /CAN Ch2/FDCAN_RX
- U11 pad 4: /CAN Ch2/CT2_AR -> GND
- U11 pad 5: ISO_2 -> /CAN Ch2/ISO
- U11 pad 6: /CAN Ch2/CT2_GR -> /CAN Ch2/CAN_L
- U11 pad 7: /CAN Ch2/CT2_GS -> /CAN Ch2/CAN_H
- U11 pad 8: +5V0_ISO_2 -> /CAN Ch2/+5V0_ISO
- U13 pad 2: FDCAN1_TX -> /CAN Ch1/FDCAN_TX
- U13 pad 3: FDCAN1_RX -> /CAN Ch1/FDCAN_RX
- U13 pad 5: ISO_1 -> /CAN Ch1/ISO
- U2 pad 33: unconnected-(U2B-VSS-Pad33) -> GND
- U3 pad 17: unconnected-(U3-VDDIO-Pad17) -> +3V3_DCDC
- U3 pad 2: unconnected-(U3-VBUS-Pad2) -> /USB/ULPI_VBUS
- U3 pad 21: unconnected-(U3-VDD1.8-Pad21) -> /USB/+1V8_ULPI
- U3 pad 22: unconnected-(U3-RESETB-Pad22) -> ULPI_RST
- U3 pad 24: unconnected-(U3-RBIAS-Pad24) -> /USB/ULPI_RBIAS
- U3 pad 3: unconnected-(U3-VBAT-Pad3) -> +3V3_DCDC
- U3 pad 4: unconnected-(U3-VDD3.3-Pad4) -> /USB/ULPI_REGOUT_3V3
- U4 pad 1: unconnected-(U4-BST-Pad1) -> /Bus Power/LV_BOOT
- U4 pad 2: unconnected-(U4-GND-Pad2) -> /Bus Power/+VIN_DB9_PR
- U4 pad 3: unconnected-(U4-FB-Pad3) -> /Bus Power/LV_EN
- U4 pad 4: unconnected-(U4-EN-Pad4) -> /Bus Power/LV_RT
- U4 pad 5: unconnected-(U4-VIN-Pad5) -> /Bus Power/LV_FB
- U4 pad 6: unconnected-(U4-LX-Pad6) -> /Bus Power/LV_SS
- U7 pad 3: +VIN_CH1 -> /Bus Power/+VIN_DB9_PR
- U8 pad 5: ISO_1 -> /CAN Ch1/ISO
